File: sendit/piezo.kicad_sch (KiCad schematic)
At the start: 5 parts, among them Q4 AO3400A

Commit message: big change removing the usb hub and serial chip.
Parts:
- renumbered Q4 to Q1, R21 to R15, R22 to R16
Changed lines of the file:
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@@
 		(on_board yes)
 		(dnp no)
-		(property "Reference" "#PWR027"
+		(property "Reference" "#PWR029"
 			(at 143.51 69.85 0)
 			(effects
@@
 			(project "sendit"
 				(path "/a355e4d0-2918-44fc-be8d-2503b84c6d6c/730ddc54-308b-4950-8f3a-2beb2098c60b"
-					(reference "#PWR027")
+					(reference "#PWR029")
 					(unit 1)
 				)
@@
 		(on_board yes)
 		(dnp no)
-		(property "Reference" "Q4"
+		(property "Reference" "Q1"
 			(at 146.05 92.71 0)
 			(effects
@@
 			(project "sendit"
 				(path "/a355e4d0-2918-44fc-be8d-2503b84c6d6c/730ddc54-308b-4950-8f3a-2beb2098c60b"
-					(reference "Q4")
+					(reference "Q1")
 					(unit 1)
 				)
@@
 		(dnp no)
 		(fields_autoplaced yes)
-		(property "Reference" "R21"
+		(property "Reference" "R15"
 			(at 128.27 87.63 90)
 			(effects
@@
 			(project "sendit"
 				(path "/a355e4d0-2918-44fc-be8d-2503b84c6d6c/730ddc54-308b-4950-8f3a-2beb2098c60b"
-					(reference "R21")
+					(reference "R15")
 					(unit 1)
 				)
@@
 		(dnp no)
 		(fields_autoplaced yes)
-		(property "Reference" "#PWR028"
+		(property "Reference" "#PWR030"
 			(at 143.51 109.22 0)
 			(effects
@@
 			(project "sendit"
 				(path "/a355e4d0-2918-44fc-be8d-2503b84c6d6c/730ddc54-308b-4950-8f3a-2beb2098c60b"
-					(reference "#PWR028")
+					(reference "#PWR030")
 					(unit 1)
 				)
@@
 		(dnp no)
 		(fields_autoplaced yes)
-		(property "Reference" "R22"
+		(property "Reference" "R16"
 			(at 135.89 97.7899 0)
 			(effects
@@
 			(project "sendit"
 				(path "/a355e4d0-2918-44fc-be8d-2503b84c6d6c/730ddc54-308b-4950-8f3a-2beb2098c60b"
-					(reference "R22")
+					(reference "R16")
 					(unit 1)
 				)

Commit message: first pass fully routed.
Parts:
- renumbered D6 to D5, R15 to R14, R16 to R15
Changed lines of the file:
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@@
 		(dnp no)
 		(fields_autoplaced yes)
-		(property "Reference" "R15"
+		(property "Reference" "R14"
 			(at 128.27 87.63 90)
 			(effects
@@
 			(project "sendit"
 				(path "/a355e4d0-2918-44fc-be8d-2503b84c6d6c/730ddc54-308b-4950-8f3a-2beb2098c60b"
-					(reference "R15")
+					(reference "R14")
 					(unit 1)
 				)
@@
 		(on_board yes)
 		(dnp no)
-		(property "Reference" "D6"
+		(property "Reference" "D5"
 			(at 139.7 78.4225 0)
 			(effects
@@
 			(project "sendit"
 				(path "/a355e4d0-2918-44fc-be8d-2503b84c6d6c/730ddc54-308b-4950-8f3a-2beb2098c60b"
-					(reference "D6")
+					(reference "D5")
 					(unit 1)
 				)
@@
 		(dnp no)
 		(fields_autoplaced yes)
-		(property "Reference" "R16"
+		(property "Reference" "R15"
 			(at 135.89 97.7899 0)
 			(effects
@@
 			(project "sendit"
 				(path "/a355e4d0-2918-44fc-be8d-2503b84c6d6c/730ddc54-308b-4950-8f3a-2beb2098c60b"
-					(reference "R16")
+					(reference "R15")
 					(unit 1)
 				)

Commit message: all footprints have 3d models now
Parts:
- BZ1: footprint Buzzer_Beeper:MagneticBuzzer_PUI_AT-0927-TT-6-R -> yarrboard:MagneticBuzzer_QMB-09B-03
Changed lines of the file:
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@@
 			)
 		)
-		(property "Footprint" "Buzzer_Beeper:MagneticBuzzer_PUI_AT-0927-TT-6-R"
+		(property "Footprint" "yarrboard:MagneticBuzzer_QMB-09B-03"
 			(at 145.415 76.2 90)
 			(effects

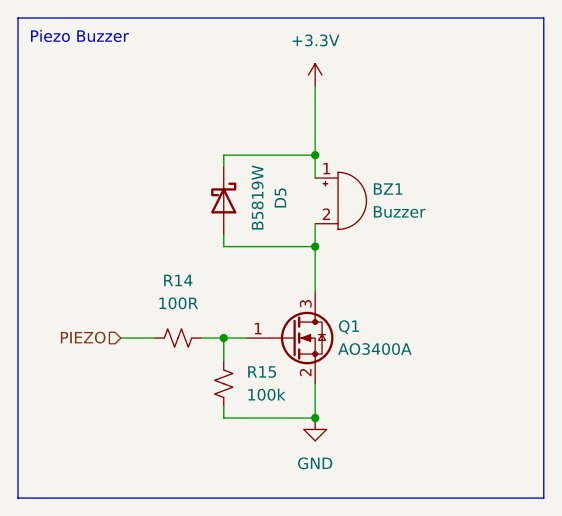
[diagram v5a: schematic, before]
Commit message: added pullup resistors to ads1115 alert line
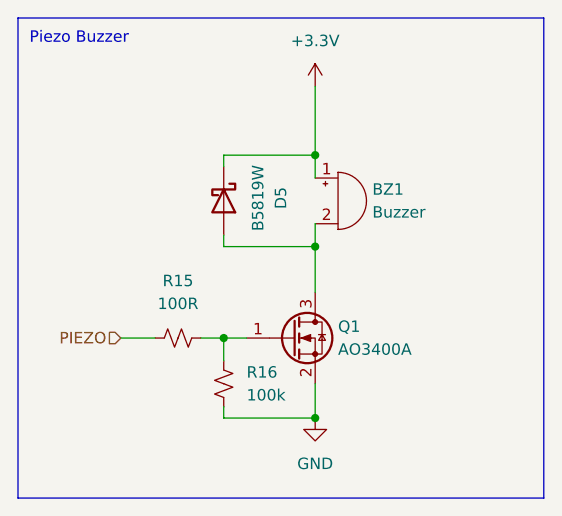
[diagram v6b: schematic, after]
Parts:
- renumbered R14 to R15, R15 to R16
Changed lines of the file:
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@@
 		(dnp no)
 		(fields_autoplaced yes)
-		(property "Reference" "R14"
+		(property "Reference" "R15"
 			(at 128.27 87.63 90)
 			(effects
@@
 			(project "sendit"
 				(path "/a355e4d0-2918-44fc-be8d-2503b84c6d6c/730ddc54-308b-4950-8f3a-2beb2098c60b"
-					(reference "R14")
+					(reference "R15")
 					(unit 1)
 				)
@@
 		(dnp no)
 		(fields_autoplaced yes)
-		(property "Reference" "R15"
+		(property "Reference" "R16"
 			(at 135.89 97.7899 0)
 			(effects
@@
 			(project "sendit"
 				(path "/a355e4d0-2918-44fc-be8d-2503b84c6d6c/730ddc54-308b-4950-8f3a-2beb2098c60b"
-					(reference "R15")
+					(reference "R16")
 					(unit 1)
 				)
